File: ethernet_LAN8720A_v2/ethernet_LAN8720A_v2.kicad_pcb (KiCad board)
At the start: 2 copper layers, 86.5 x 61 mm, 46 parts, among them P1 SI-52003-F, P3 PoE, U1 LAN8720A-CP, U2 ASV-50.000MHZ-E-T

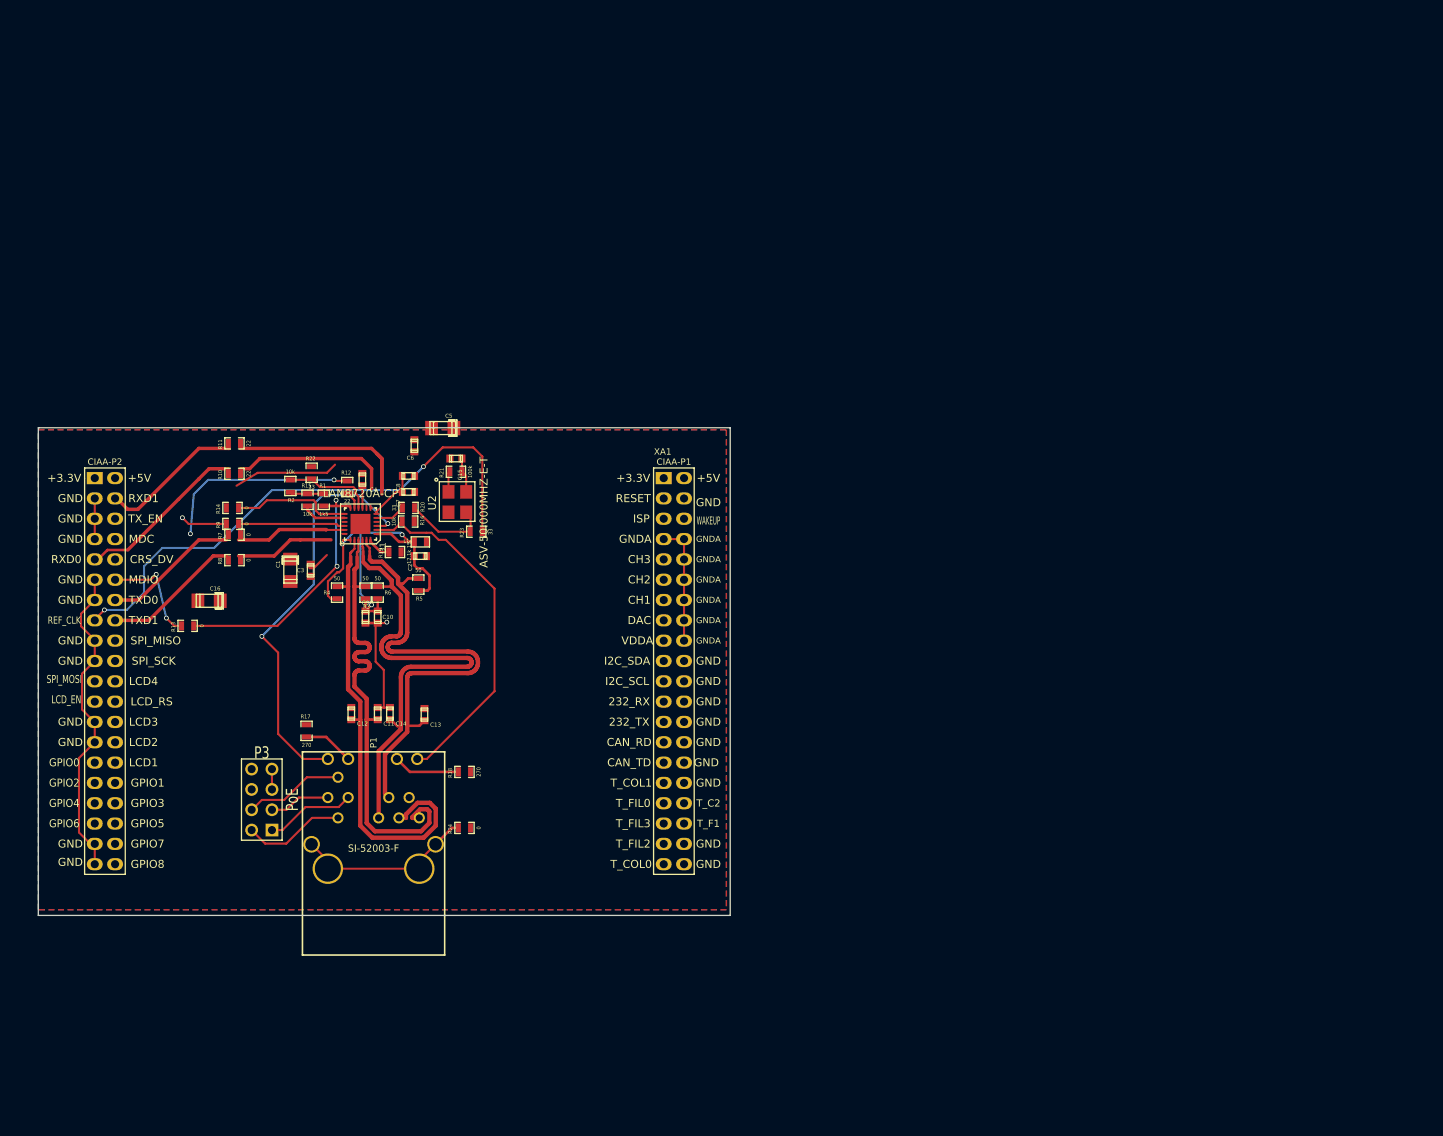
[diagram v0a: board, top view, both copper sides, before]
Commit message: Acomodo el PCB para Poncho Izquierdo. Borde PCB para ver LEDs. Borro ruteos corridos. Agrego footprints plantilla EDU-CIAA.
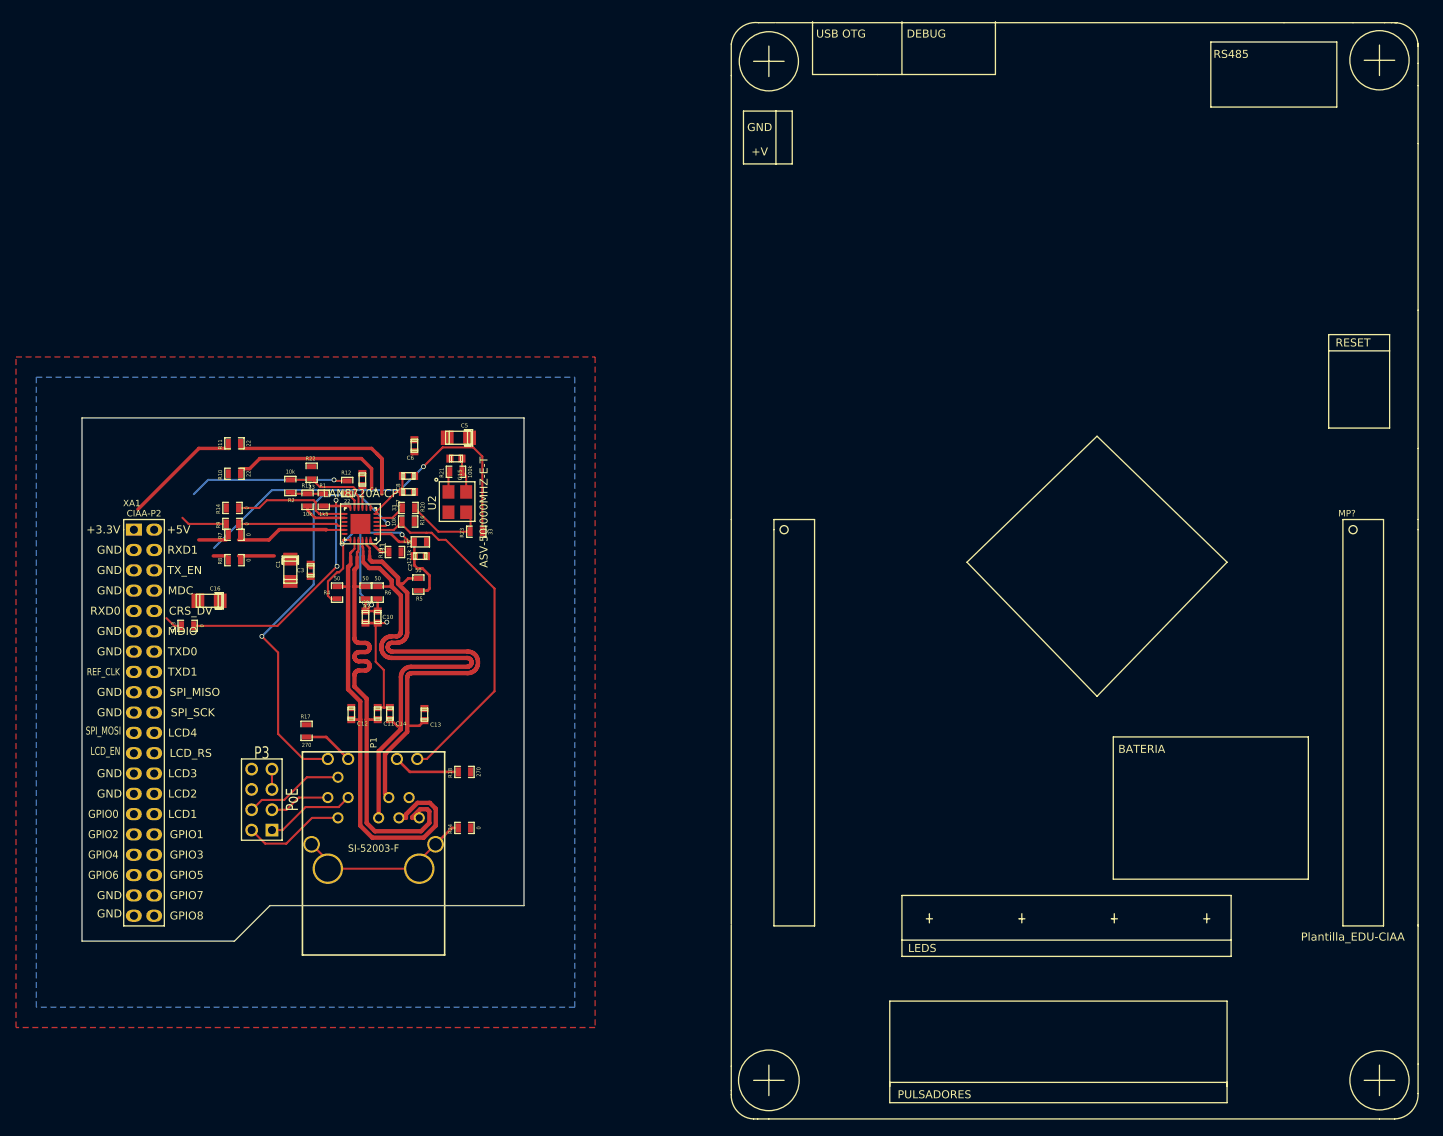
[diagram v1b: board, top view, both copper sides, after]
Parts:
- added MP?: Plantilla_EDU-CIAA, eth:Plantilla_EDU-CIAA, F.Cu at (250.1, 82.7)
- XA1: footprint eth:Conn_Poncho_Chico -> eth:Conn_Poncho_Izquierdo
- moved XA1 66.5 mm to (97.7, 82.7)
- moved C5 2.30 mm to (138.2, 71.2)
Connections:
- P3 pad 6: (no net) -> Net-(P3-Pad6)
- U1 pad 15: (no net) -> /Circuito Principal/PHY_nRESET
- U1 pad 4: (no net) -> Net-(U1-Pad4)
- XA1 pad 41: (no net) -> +3.3V
- XA1 pad 42: (no net) -> +5V
- XA1 pad 58: (no net) -> /Circuito Principal/MISO
- XA1 pad 60: (no net) -> /Circuito Principal/spiSCK
- XA1 pad 61: (no net) -> /Circuito Principal/MOSI
- XA1 pad 62: (no net) -> /Circuito Principal/LCD4
- XA1 pad 63: (no net) -> /Circuito Principal/LCD_EN
- XA1 pad 64: (no net) -> /Circuito Principal/RS
- XA1 pad 66: (no net) -> /Circuito Principal/LCD3
- XA1 pad 68: (no net) -> /Circuito Principal/LCD2
- XA1 pad 69: (no net) -> /Circuito Principal/GPIO0
- XA1 pad 70: (no net) -> /Circuito Principal/LCD1
- XA1 pad 71: (no net) -> /Circuito Principal/GPIO2
- XA1 pad 72: (no net) -> /Circuito Principal/GPIO1
- XA1 pad 73: (no net) -> /Circuito Principal/GPIO4
- XA1 pad 74: (no net) -> /Circuito Principal/GPIO3
- XA1 pad 75: (no net) -> /Circuito Principal/GPIO6
- XA1 pad 76: (no net) -> /Circuito Principal/GPIO5
- XA1 pad 78: (no net) -> /Circuito Principal/GPIO7
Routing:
- net /Circuito Principal/RCLK: track 69.3 -> 18.2 mm, vias 2 -> 1
- net (no net): track 16.0 -> 66.9 mm
- net GND: track 63.2 -> 17.9 mm
- net Net-(R11-Pad2): track 28.7 -> 0.51 mm
- net Net-(R10-Pad2): track 20.0 -> 0.00 mm
- net /Circuito Principal/RXD1: track 18.1 -> 0.00 mm
- net /Circuito Principal/TXD0: track 17.0 -> 0.00 mm
- net /Circuito Principal/TXD1: track 17.2 -> 1.64 mm
- net GNDA: track 15.2 -> 0.00 mm
- net /Circuito Principal/MDIO: track 13.3 -> 0.92 mm, vias 2 -> 0
- net /Circuito Principal/RXD0: track 21.4 -> 30.4 mm
- net Net-(R8-Pad2): track 12.4 -> 4.46 mm
- net /Circuito Principal/CRS: track 24.9 -> 20.0 mm, vias 2 -> 1
- net /Circuito Principal/TXEN: track 5.82 -> 7.19 mm, vias 1 -> 0
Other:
- board size 86.5 x 61 mm -> 55.2 x 65.4 mm

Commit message: Redibujo planos, agrego keepout en diferenciales, quito rulo grande en diferencial, muevo oscilador 50MHZ entre PHY y MAC, muevo capacitores filtro 3.3v.
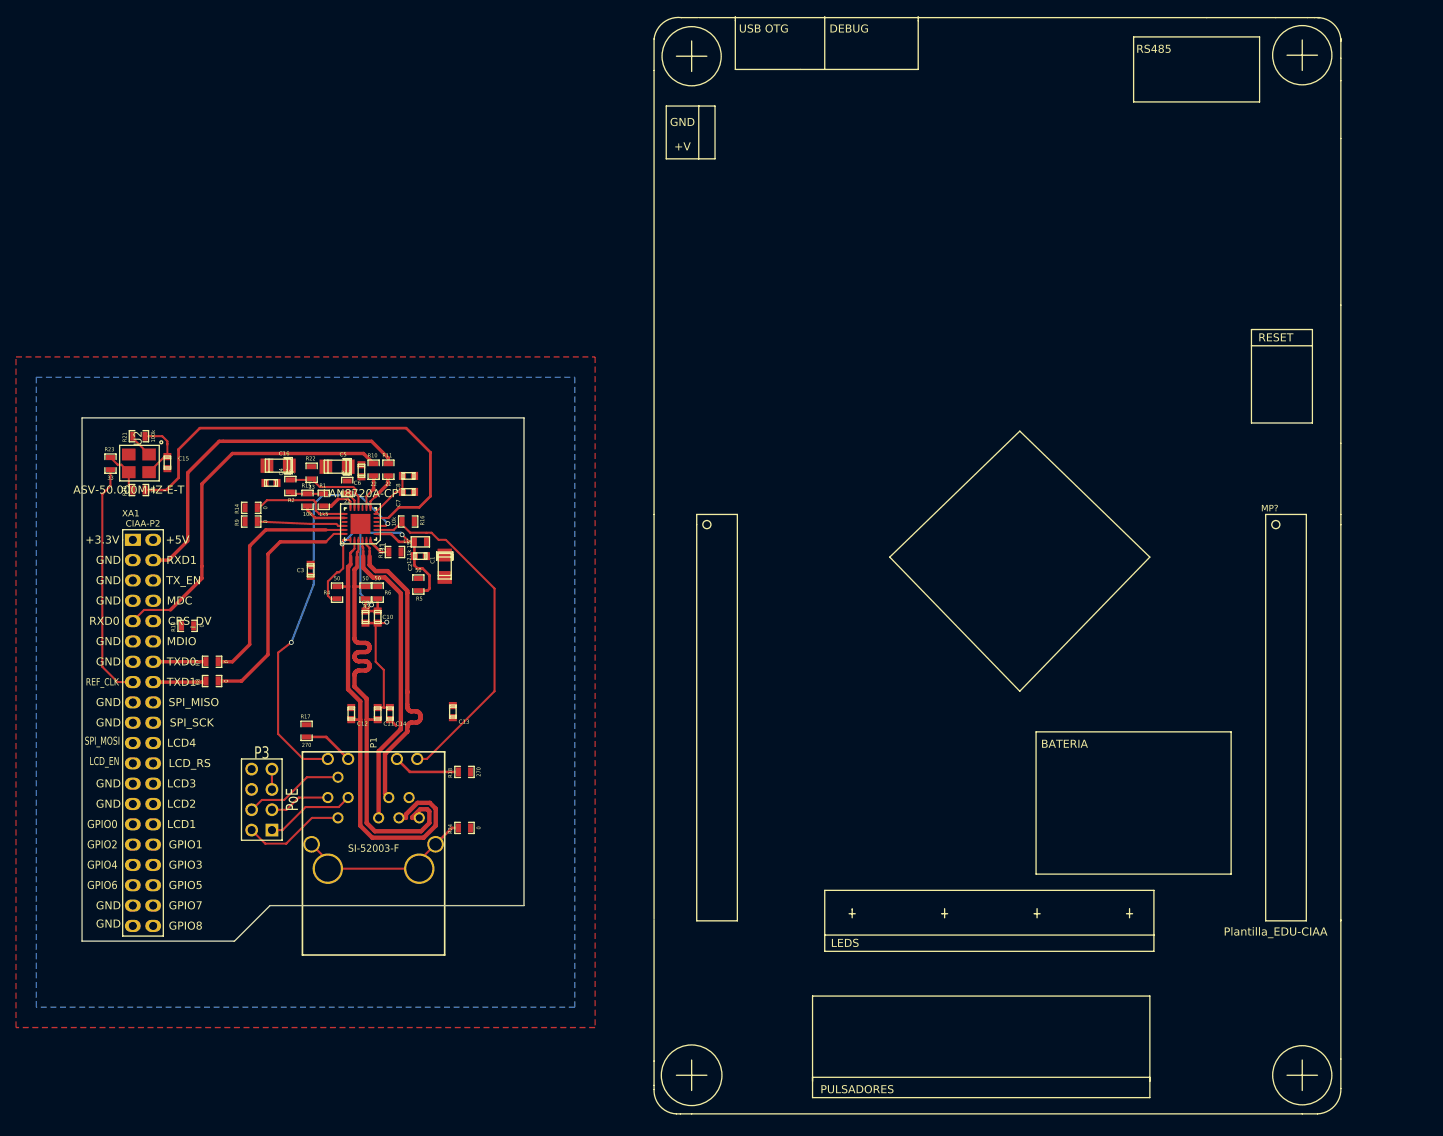
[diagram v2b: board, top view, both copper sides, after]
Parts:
- moved R23 46.5 mm to (94.8, 74.5), turned to 270 degrees
- moved R21 39.9 mm to (98.3, 71.0)
- moved U2 37.7 mm to (99.6, 73.3), turned to 180 degrees
- moved C15 36.1 mm to (101.9, 74.3), turned to 90 degrees
- moved R20 33.8 mm to (98.3, 77.8), turned to 0 degrees
- moved R11 19.5 mm to (129.5, 75.2), turned to 270 degrees
- moved C1 19.3 mm to (136.5, 87.3)
- moved C16 19.0 mm to (115.7, 74.7)
- moved R10 17.4 mm to (127.6, 75.2), turned to 270 degrees
- moved R7 16.1 mm to (107.5, 99.2)
- moved C5 15.6 mm to (123.1, 74.8)
- moved R8 15.4 mm to (107.5, 101.6)
- moved C4 11.4 mm to (114.8, 76.9), turned to 0 degrees
- moved MP? 9.67 mm to (240.4, 82.1)
- moved C6 7.32 mm to (126.1, 75.4)
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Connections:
- P3 pad 6: Net-(P3-Pad6) -> (no net)
- U1 pad 15: /Circuito Principal/PHY_nRESET -> (no net)
- U1 pad 4: Net-(U1-Pad4) -> (no net)
- XA1 pad 58: /Circuito Principal/MISO -> (no net)
- XA1 pad 60: /Circuito Principal/spiSCK -> (no net)
- XA1 pad 61: /Circuito Principal/MOSI -> (no net)
- XA1 pad 62: /Circuito Principal/LCD4 -> (no net)
- XA1 pad 63: /Circuito Principal/LCD_EN -> (no net)
- XA1 pad 64: /Circuito Principal/RS -> (no net)
- XA1 pad 66: /Circuito Principal/LCD3 -> (no net)
- XA1 pad 68: /Circuito Principal/LCD2 -> (no net)
- XA1 pad 69: /Circuito Principal/GPIO0 -> (no net)
- XA1 pad 70: /Circuito Principal/LCD1 -> (no net)
- XA1 pad 71: /Circuito Principal/GPIO2 -> (no net)
- XA1 pad 72: /Circuito Principal/GPIO1 -> (no net)
- XA1 pad 73: /Circuito Principal/GPIO4 -> (no net)
- XA1 pad 74: /Circuito Principal/GPIO3 -> (no net)
- XA1 pad 75: /Circuito Principal/GPIO6 -> (no net)
- XA1 pad 76: /Circuito Principal/GPIO5 -> (no net)
- XA1 pad 78: /Circuito Principal/GPIO7 -> (no net)
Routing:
- net Net-(R20-Pad2): track 3.76 -> 103.1 mm
- net (no net): track 66.9 -> 0.50 mm
- net /Circuito Principal/RXD1: track 0.00 -> 42.1 mm
- net Net-(R1-Pad2): track 34.0 -> 4.61 mm, vias 2 -> 0
- net Net-(R8-Pad2): track 4.46 -> 30.8 mm
- net /Circuito Principal/Rx_P: track 61.8 -> 38.8 mm
- net /Circuito Principal/Rx_N: track 62.0 -> 39.9 mm
- net /Circuito Principal/CRS: track 20.0 -> 0.00 mm, vias 1 -> 0
- net /Circuito Principal/RXD0: track 30.4 -> 46.2 mm
- net /Circuito Principal/RCLK: track 18.2 -> 29.7 mm, vias 1 -> 0
- net Net-(R7-Pad2): track 21.5 -> 29.8 mm
- net /Circuito Principal/TXEN: track 7.19 -> 0.00 mm
- net /Circuito Principal/TXD0: track 0.00 -> 6.60 mm
- net Net-(R20-Pad1): track 10.9 -> 5.49 mm
- net /Circuito Principal/TXD1: track 1.64 -> 6.66 mm
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
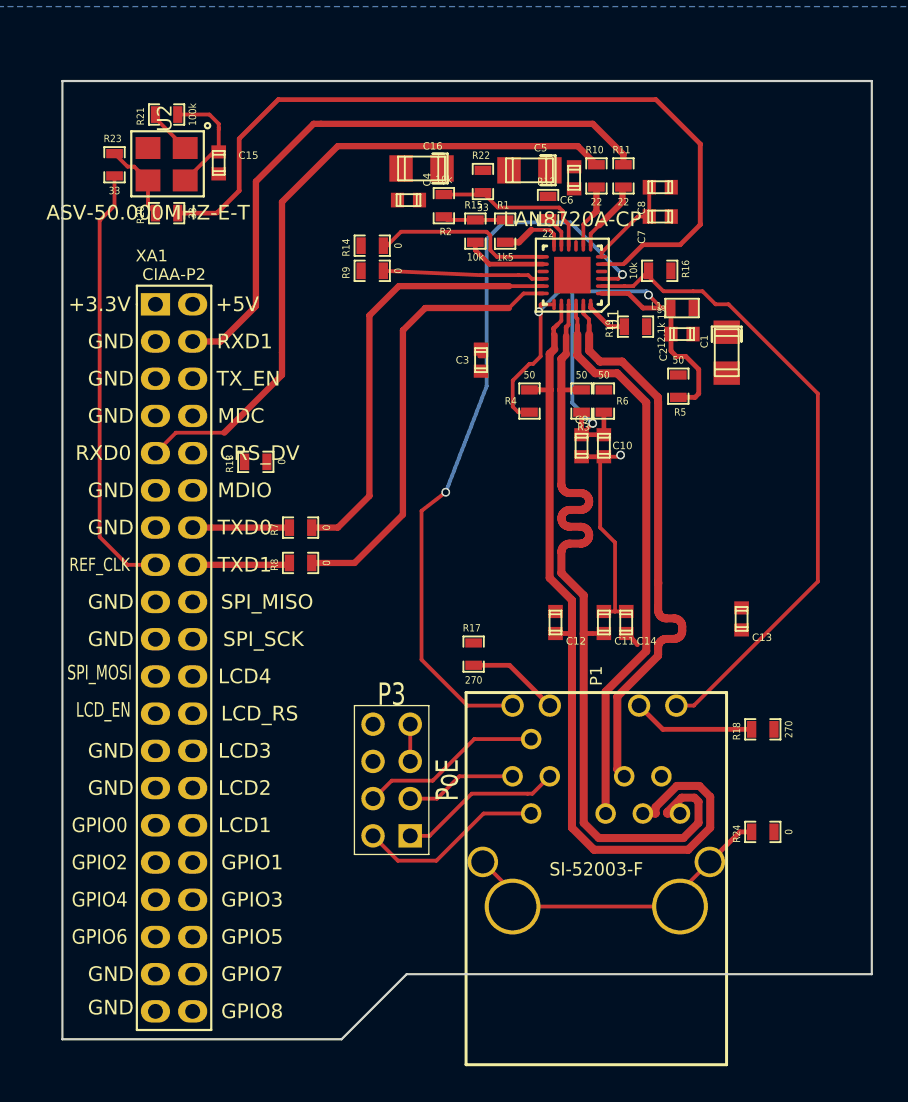
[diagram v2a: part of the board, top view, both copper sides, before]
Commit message: Ruteo de todas las lineas restantes luego de RMII y conexión solo izquierda.
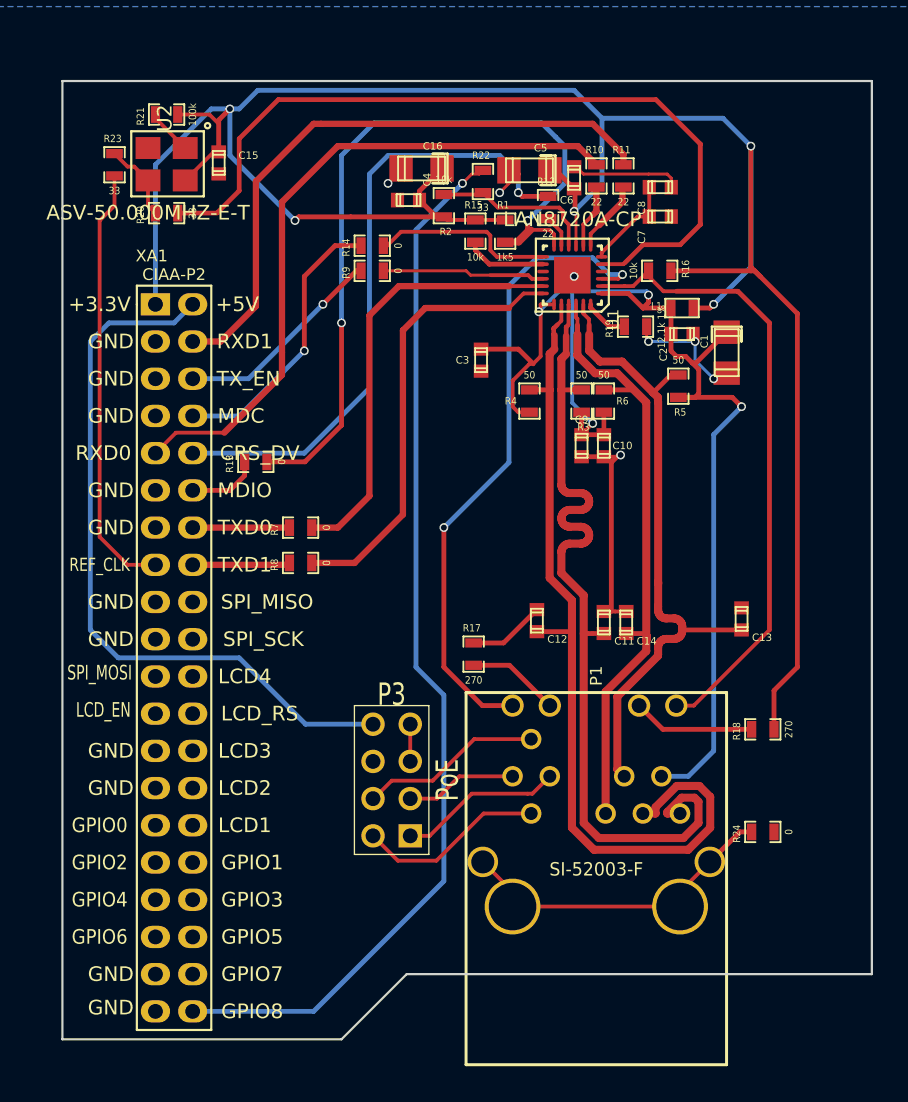
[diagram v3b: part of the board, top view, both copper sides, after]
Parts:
- moved C12 1.28 mm to (123.6, 105.6)
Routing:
- net +3.3V: track 12.6 -> 171.0 mm, vias 0 -> 5
- net /Circuito Principal/GPIO8: track 0.00 -> 72.3 mm, vias 0 -> 1
- net Net-(R1-Pad2): track 4.61 -> 54.6 mm, vias 0 -> 2
- net +5V: track 0.00 -> 49.7 mm
- net /Circuito Principal/CRS: track 0.00 -> 43.1 mm, vias 0 -> 1
- net Net-(C1-Pad1): track 49.3 -> 89.0 mm, vias 3 -> 4
- net GND: track 18.1 -> 43.5 mm, vias 1 -> 7
- net /Circuito Principal/MDC: track 0.00 -> 19.3 mm, vias 0 -> 1
- net /Circuito Principal/TXEN: track 0.00 -> 14.5 mm, vias 0 -> 1
- net /Circuito Principal/Rx_P: track 38.8 -> 45.1 mm
- net /Circuito Principal/LED_LINK: track 50.3 -> 44.2 mm
- net /Circuito Principal/MDIO: track 0.00 -> 4.91 mm
- net /Circuito Principal/Rx_N: track 39.9 -> 43.4 mm
- net /Circuito Principal/LED_100M: track 44.9 -> 43.0 mm
- net /Circuito Principal/Tx_N: track 59.2 -> 60.6 mm
